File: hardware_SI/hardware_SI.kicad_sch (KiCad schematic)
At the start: 2 parts, among them U1 OMEGA2+

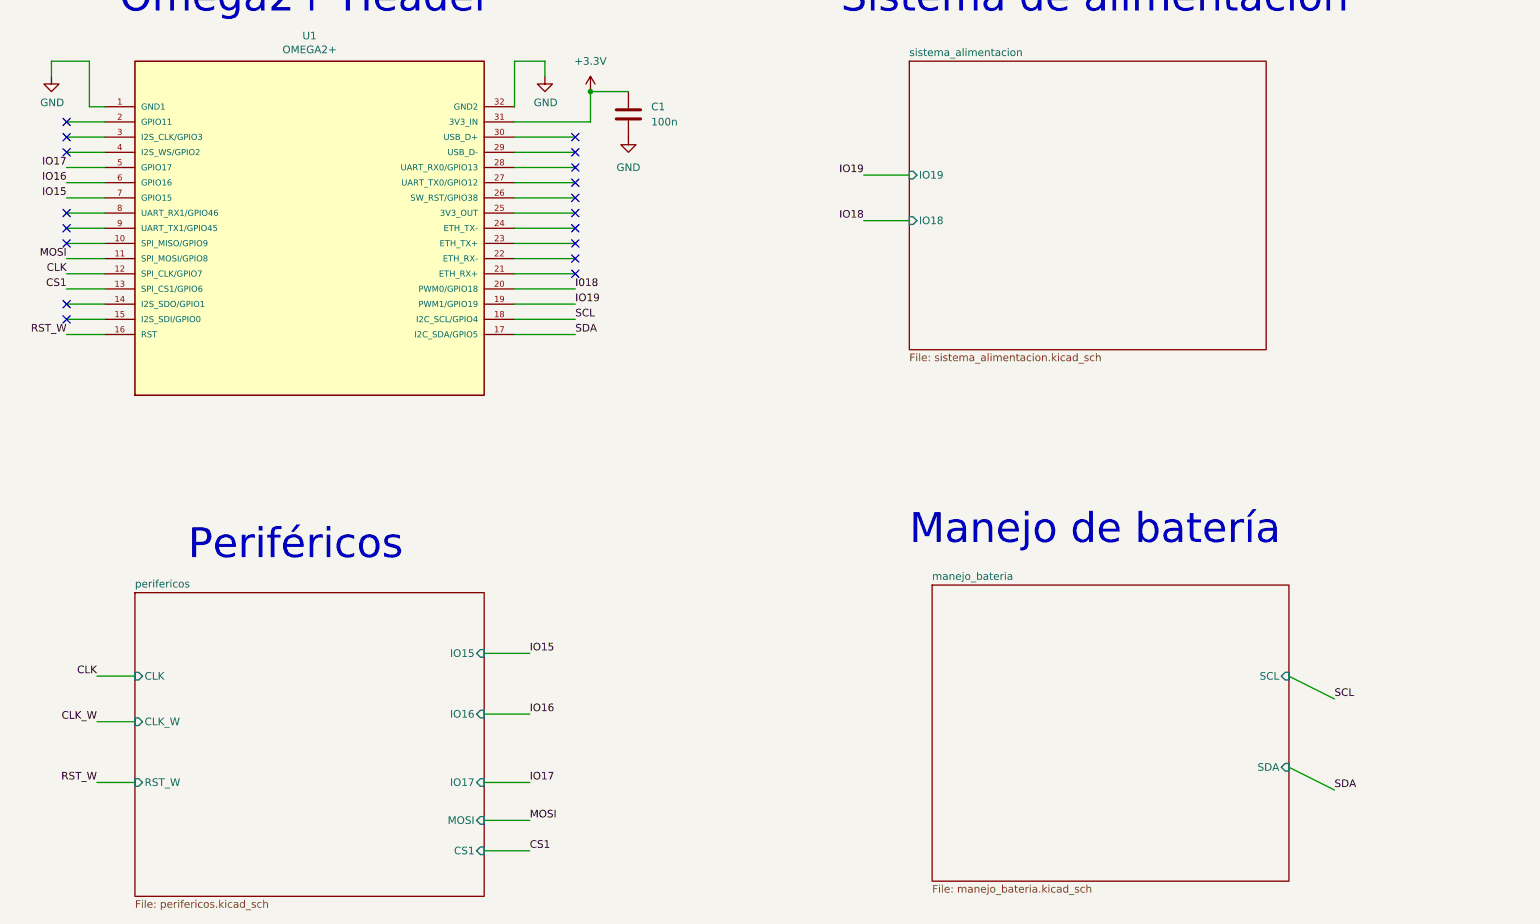
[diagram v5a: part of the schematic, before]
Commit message: mod_WD, etiquetas y clocks
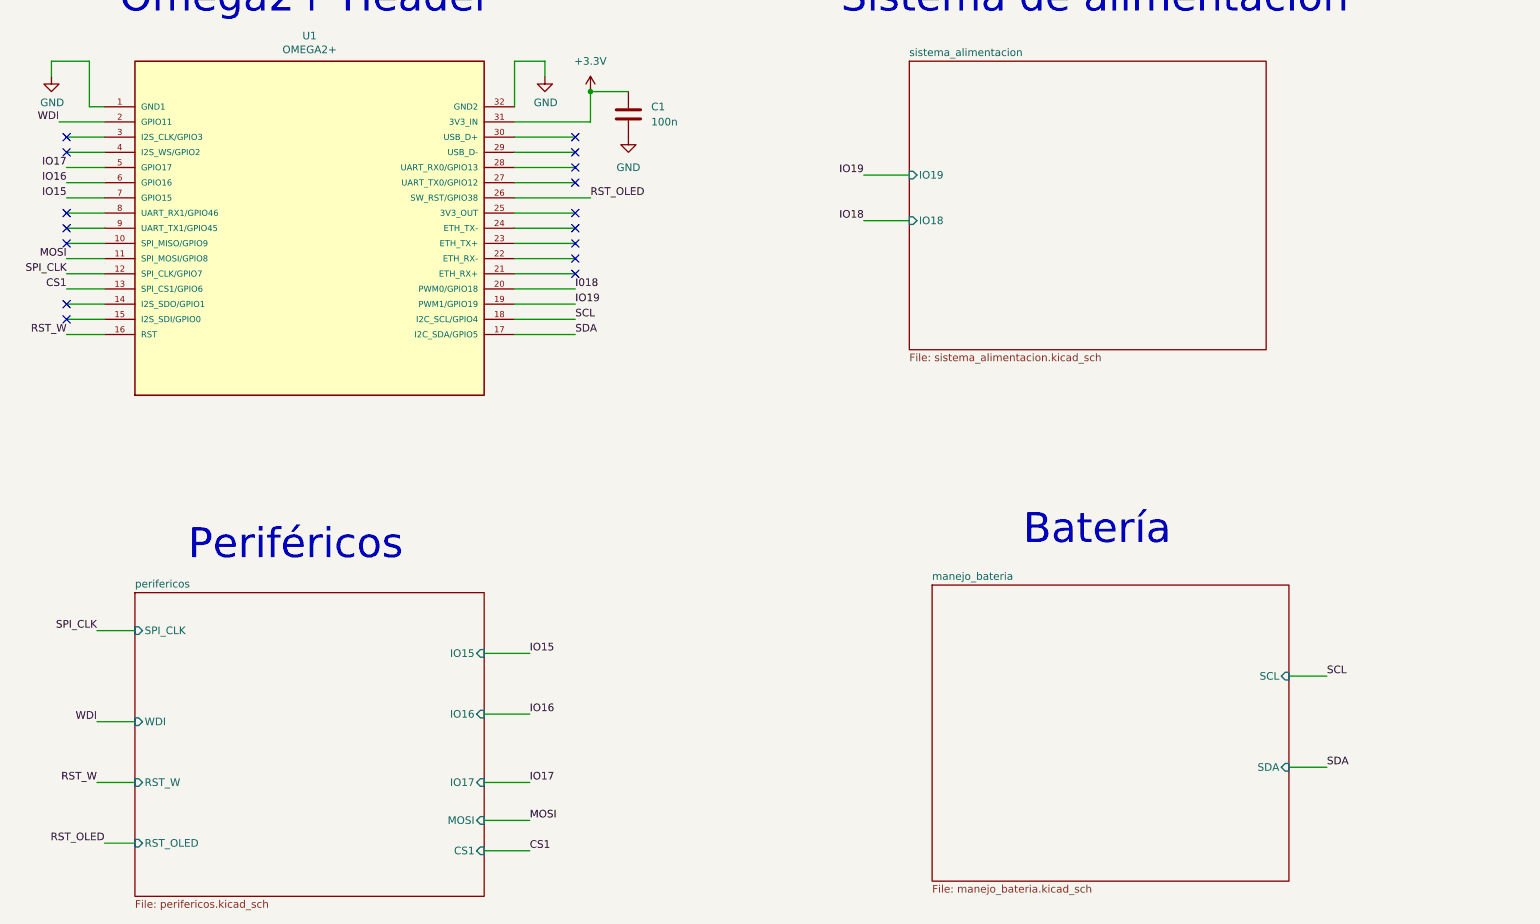
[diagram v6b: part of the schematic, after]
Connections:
- net WDI: now reaches U1.2 (GPIO11)
- net RST_OLED: now reaches U1.26 (SW_RST/GPIO38)
- net CLK renamed SPI_CLK
- no-connect marks 18 -> 16
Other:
- sheet perifericos ports: added RST_OLED, SPI_CLK, WDI; removed CLK, CLK_W
- note added: "Batería"
- note removed: "Manejo de batería"
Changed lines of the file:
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@@
   (no_connect (at 99.06 113.03))
   (no_connect (at 99.06 115.57))
-  (no_connect (at 99.06 82.55))
   (no_connect (at 99.06 85.09))
   (no_connect (at 99.06 87.63))
   (no_connect (at 184.15 107.95))
-  (no_connect (at 184.15 95.25))
   (no_connect (at 184.15 92.71))
   (no_connect (at 184.15 90.17))
@@
     (stroke (width 0) (type default) (color 0 0 0 0))
   )
-  (wire (pts (xy 173.99 95.25) (xy 184.15 95.25))
-    (stroke (width 0) (type default) (color 0 0 0 0))
-  )
   (wire (pts (xy 173.99 102.87) (xy 184.15 102.87))
     (stroke (width 0) (type default) (color 0 0 0 0))
@@
     (stroke (width 0) (type default) (color 0 0 0 0))
   )
-  (wire (pts (xy 99.06 82.55) (xy 105.41 82.55))
-    (stroke (width 0) (type default) (color 0 0 0 0))
-  )
   (wire (pts (xy 102.87 72.39) (xy 96.52 72.39))
     (stroke (width 0) (type default) (color 0 0 0 0))
@@
     (stroke (width 0) (type default) (color 0 0 0 0))
   )
-  (wire (pts (xy 303.53 175.26) (xy 311.15 179.07))
+  (wire (pts (xy 303.53 175.26) (xy 309.88 175.26))
     (stroke (width 0) (type default) (color 0 0 0 0))
   )
@@
     (stroke (width 0) (type default) (color 0 0 0 0))
   )
-  (wire (pts (xy 104.14 175.26) (xy 110.49 175.26))
+  (wire (pts (xy 173.99 95.25) (xy 186.69 95.25))
     (stroke (width 0) (type default) (color 0 0 0 0))
   )
@@
     (stroke (width 0) (type default) (color 0 0 0 0))
   )
-  (wire (pts (xy 303.53 190.5) (xy 311.15 194.31))
+  (wire (pts (xy 303.53 190.5) (xy 309.88 190.5))
     (stroke (width 0) (type default) (color 0 0 0 0))
   )
@@
     (stroke (width 0) (type default) (color 0 0 0 0))
   )
+  (wire (pts (xy 105.41 203.2) (xy 110.49 203.2))
+    (stroke (width 0) (type default) (color 0 0 0 0))
+  )
   (wire (pts (xy 173.99 110.49) (xy 184.15 110.49))
     (stroke (width 0) (type default) (color 0 0 0 0))
@@
     (stroke (width 0) (type default) (color 0 0 0 0))
   )
+  (wire (pts (xy 97.79 82.55) (xy 105.41 82.55))
+    (stroke (width 0) (type default) (color 0 0 0 0))
+  )
   (wire (pts (xy 104.14 193.04) (xy 110.49 193.04))
     (stroke (width 0) (type default) (color 0 0 0 0))
@@
   )
   (wire (pts (xy 173.99 82.55) (xy 186.69 82.55))
+    (stroke (width 0) (type default) (color 0 0 0 0))
+  )
+  (wire (pts (xy 104.14 167.64) (xy 110.49 167.64))
     (stroke (width 0) (type default) (color 0 0 0 0))
   )
@@
     (effects (font (size 5 5)) (justify left bottom))
   )
-  (text "Manejo de batería" (at 240.03 153.67 0)
+  (text "Batería" (at 259.08 153.67 0)
     (effects (font (size 5 5)) (justify left bottom))
   )
+  (label "RST_OLED" (at 186.69 95.25 0)
+    (effects (font (size 1.27 1.27)) (justify left bottom))
+  )
   (label "RST_W" (at 99.06 118.11 180)
     (effects (font (size 1.27 1.27)) (justify right bottom))
@@
     (effects (font (size 1.27 1.27)) (justify left bottom))
   )
-  (label "CLK_W" (at 104.14 182.88 180)
+  (label "WDI" (at 104.14 182.88 180)
     (effects (font (size 1.27 1.27)) (justify right bottom))
   )
@@
     (effects (font (size 1.27 1.27)) (justify left bottom))
   )
-  (label "SCL" (at 311.15 179.07 0)
+  (label "SCL" (at 309.88 175.26 0)
     (effects (font (size 1.27 1.27)) (justify left bottom))
   )
@@
     (effects (font (size 1.27 1.27)) (justify left bottom))
   )
-  (label "SDA" (at 311.15 194.31 0)
+  (label "SDA" (at 309.88 190.5 0)
     (effects (font (size 1.27 1.27)) (justify left bottom))
   )
@@
     (effects (font (size 1.27 1.27)) (justify left bottom))
   )
+  (label "RST_OLED" (at 105.41 203.2 180)
+    (effects (font (size 1.27 1.27)) (justify right bottom))
+  )
   (label "CS1" (at 99.06 110.49 180)
     (effects (font (size 1.27 1.27)) (justify right bottom))
   )
-  (label "CLK" (at 104.14 175.26 180)
+  (label "SPI_CLK" (at 104.14 167.64 180)
     (effects (font (size 1.27 1.27)) (justify right bottom))
   )
@@
     (effects (font (size 1.27 1.27)) (justify right bottom))
   )
-  (label "CLK" (at 99.06 107.95 180)
+  (label "SPI_CLK" (at 99.06 107.95 180)
+    (effects (font (size 1.27 1.27)) (justify right bottom))
+  )
+  (label "WDI" (at 97.79 82.55 180)
     (effects (font (size 1.27 1.27)) (justify right bottom))
   )
@@
       (effects (font (size 1.27 1.27)) (justify left bottom) hide)
     )
-    (property "Datasheet" "" (id 3) (at 138.43 113.03 0)
+    (property "Datasheet" "https://s3.us-west-2.amazonaws.com/secure.notion-static.com/28718f9b-350a-4ebf-9c7b-f758d83f3f79/Omega2_Datasheet.pdf?X-Amz-Algorithm=AWS4-HMAC-SHA256&X-Amz-Content-Sha256=UNSIGNED-PAYLOAD&X-Amz-Credential=AKIAT73L2G45EIPT3X45%2F20220516%2Fus-west-2%2Fs3%2Faws4_request&X-Amz-Date=20220516T163604Z&X-Amz-Expires=86400&X-Amz-Signature=d8703c4ca72b362825af5130e1190c33926a0e29ee1d94b03f16a478de49cab4&X-Amz-SignedHeaders=host&response-content-disposition=filename%20%3D%22Omega2%2520Datasheet.pdf%22&x-id=GetObject" (id 3) (at 138.43 113.03 0)
       (effects (font (size 1.27 1.27)) (justify left bottom) hide)
     )
@@
       (effects (font (size 1.27 1.27)) (justify right))
     )
-    (pin "CLK" input (at 110.49 175.26 180)
-      (effects (font (size 1.27 1.27)) (justify left))
-    )
     (pin "RST_W" input (at 110.49 193.04 180)
       (effects (font (size 1.27 1.27)) (justify left))
@@
       (effects (font (size 1.27 1.27)) (justify right))
     )
-    (pin "CLK_W" input (at 110.49 182.88 180)
+    (pin "RST_OLED" input (at 110.49 203.2 180)
+      (effects (font (size 1.27 1.27)) (justify left))
+    )
+    (pin "WDI" input (at 110.49 182.88 180)
+      (effects (font (size 1.27 1.27)) (justify left))
+    )
+    (pin "SPI_CLK" input (at 110.49 167.64 180)
       (effects (font (size 1.27 1.27)) (justify left))
     )
@@
       (reference "#PWR0120") (unit 1) (value "GND") (footprint "")
     )
-    (path "/0b6e3c2b-d039-4782-bbc3-fab07ed657e7/07eb388f-4b3a-4124-b604-f7295f2dea93"
-      (reference "#PWR?") (unit 1) (value "GND") (footprint "")
-    )
     (path "/d17f886c-ddbc-4da5-b4ad-887fd41c7d7b/086281b8-3cab-4f61-8733-81d3fd71bf66"
       (reference "#PWR?") (unit 1) (value "GND") (footprint "")
@@
       (reference "#PWR?") (unit 1) (value "GND") (footprint "")
     )
+    (path "/0b6e3c2b-d039-4782-bbc3-fab07ed657e7/67537f00-4c81-4a6c-b687-e5391ecd31ce"
+      (reference "#PWR?") (unit 1) (value "+3.3V") (footprint "")
+    )
     (path "/0b6e3c2b-d039-4782-bbc3-fab07ed657e7/6812a301-f067-48ee-9f8c-c2c15202b1ec"
       (reference "#PWR?") (unit 1) (value "GND") (footprint "")
@@
       (reference "#PWR?") (unit 1) (value "+BATT") (footprint "")
     )
-    (path "/0b6e3c2b-d039-4782-bbc3-fab07ed657e7/89b67c4b-2345-4691-ae88-36a913a6bf35"
-      (reference "#PWR?") (unit 1) (value "GND") (footprint "")
-    )
     (path "/0b6e3c2b-d039-4782-bbc3-fab07ed657e7/8c8ec256-d623-4d05-8118-ede844e36bd8"
       (reference "#PWR?") (unit 1) (value "GND") (footprint "")
@@
       (reference "C2") (unit 1) (value "100n") (footprint "")
     )
-    (path "/0b6e3c2b-d039-4782-bbc3-fab07ed657e7/28be84aa-b431-4431-8eeb-d676de337ffa"
-      (reference "C3") (unit 1) (value "100n") (footprint "")
-    )
     (path "/0b6e3c2b-d039-4782-bbc3-fab07ed657e7/05cf4233-8f27-418a-a330-7ad49b161d28"
       (reference "C4") (unit 1) (value "100n") (footprint "")
@@
     )
     (path "/d17f886c-ddbc-4da5-b4ad-887fd41c7d7b/361394dc-edd8-4eab-92b4-34d2946ee54c"
-      (reference "FB1") (unit 1) (value "FerriteBead") (footprint "")
+      (reference "FB1") (unit 1) (value "FerriteBead") (footprint "Resistor_SMD:R_0805_2012Metric_Pad1.20x1.40mm_HandSolder")
+    )
+    (path "/d17f886c-ddbc-4da5-b4ad-887fd41c7d7b/2b53b09c-0453-4d12-8b2d-cd4bbef34be2"
+      (reference "FB?") (unit 1) (value "FerriteBead") (footprint "Resistor_SMD:R_0805_2012Metric_Pad1.20x1.40mm_HandSolder")
     )
     (path "/0b6e3c2b-d039-4782-bbc3-fab07ed657e7/fa617b97-2321-4c58-84fc-0275fff3eb00"
@@
       (reference "R13") (unit 1) (value "8M") (footprint "Resistor_SMD:R_0805_2012Metric_Pad1.20x1.40mm_HandSolder")
     )
+    (path "/0b6e3c2b-d039-4782-bbc3-fab07ed657e7/b71d969a-cf4e-4262-a844-fa6303e4c8d1"
+      (reference "R?") (unit 1) (value "10k") (footprint "Resistor_SMD:R_0805_2012Metric_Pad1.20x1.40mm_HandSolder")
+    )
     (path "/d17f886c-ddbc-4da5-b4ad-887fd41c7d7b/ab8397f0-cb8b-42a3-97b6-8f2bb790bc88"

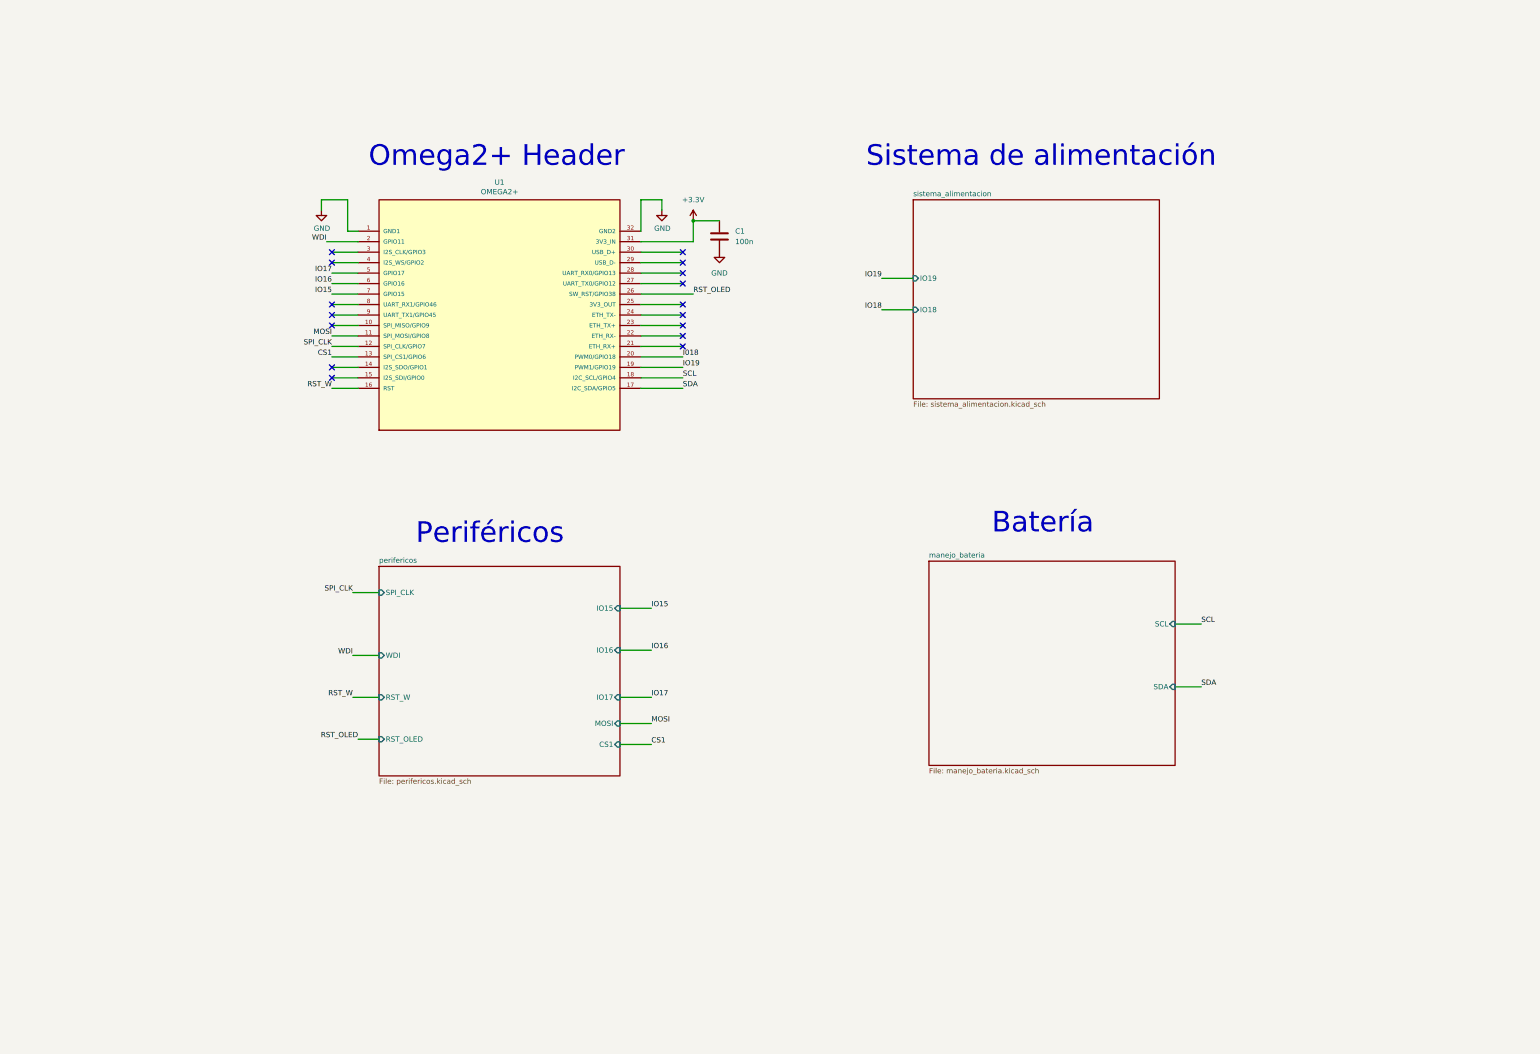
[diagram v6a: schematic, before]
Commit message: USB Serial, huellas y correcciones ERC
- Se agregaron componentes para la comunicación serial con la Omega2+.
- Se actualizaron huellas en función de la disponibilidad de los componentes.
- Se ejecutó el ERC y se solucionaron los errores mostrados.
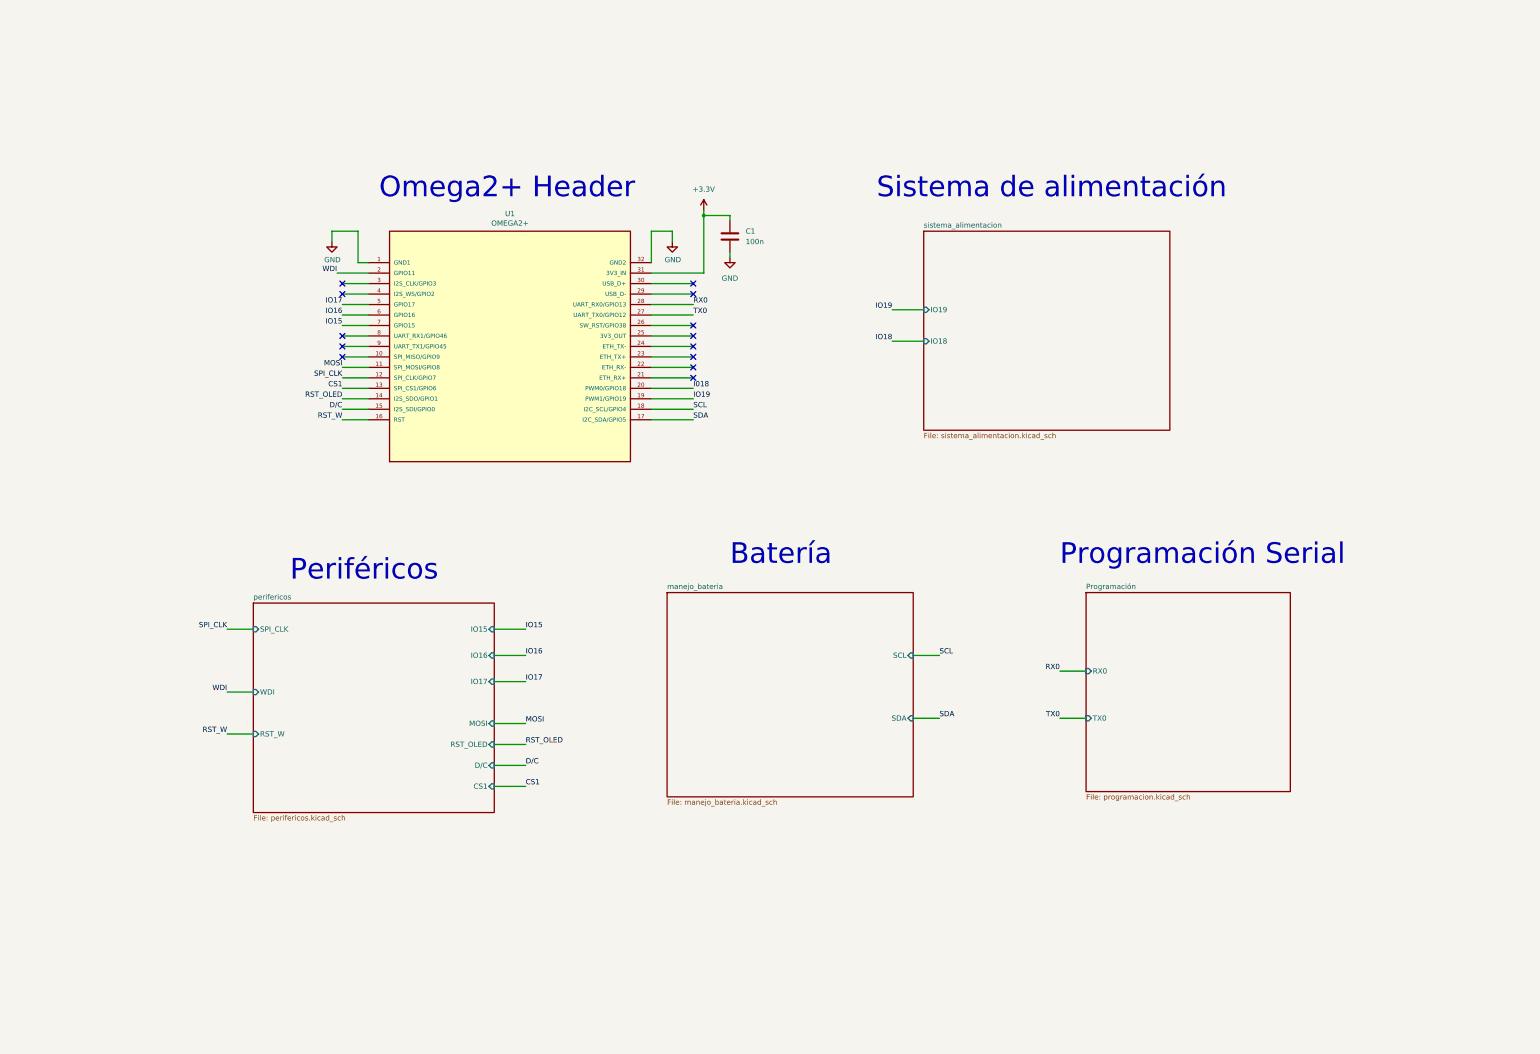
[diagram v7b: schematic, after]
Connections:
- net RST_OLED: now also U1.14 (I2S_SDO/GPIO1); no longer U1.26 (SW_RST/GPIO38)
- net D/C: now reaches U1.15 (I2S_SDI/GPIO0)
- net TX0: now reaches U1.27 (UART_TX0/GPIO12)
- net RX0: now reaches U1.28 (UART_RX0/GPIO13)
- no-connect marks 16 -> 13
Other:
- added sheet Programación (programacion.kicad_sch)
- sheet perifericos ports: added D/C; removed none
- note added: "Programación Serial"
- moved on the sheet: C1, U1
